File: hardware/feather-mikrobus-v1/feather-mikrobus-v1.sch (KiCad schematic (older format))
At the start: 24 parts, among them J1 Adafruit_Feather_socket_heade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, J2 Adafruit_Feather_socket_heade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, J3 mikroBUS_socket_header_left_p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, J4 mikroBUS_socket_header_right_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, SW1 C_and_K_JS102011SAQN, SW2 C_and_K_KMR421GULCLFS, SW3 C_and_K_KMR421GULCLFS

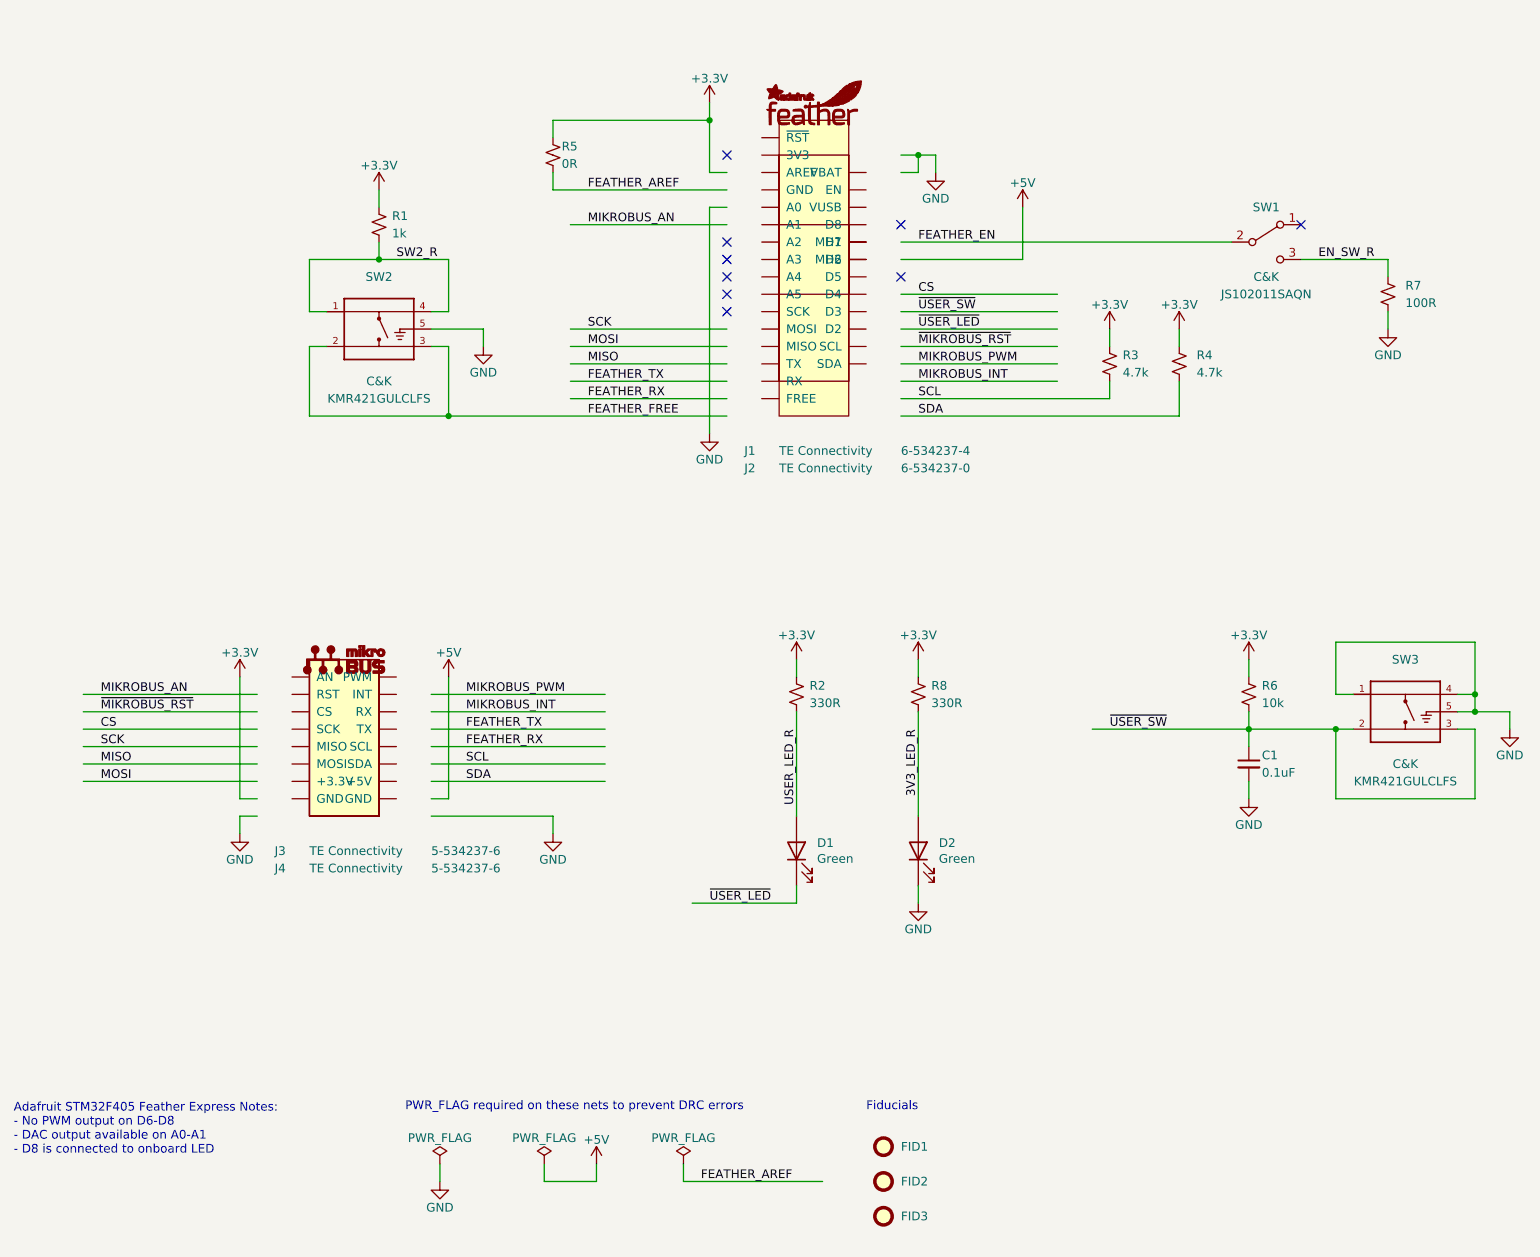
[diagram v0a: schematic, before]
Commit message: Update schematic to use new symbols and worksheet
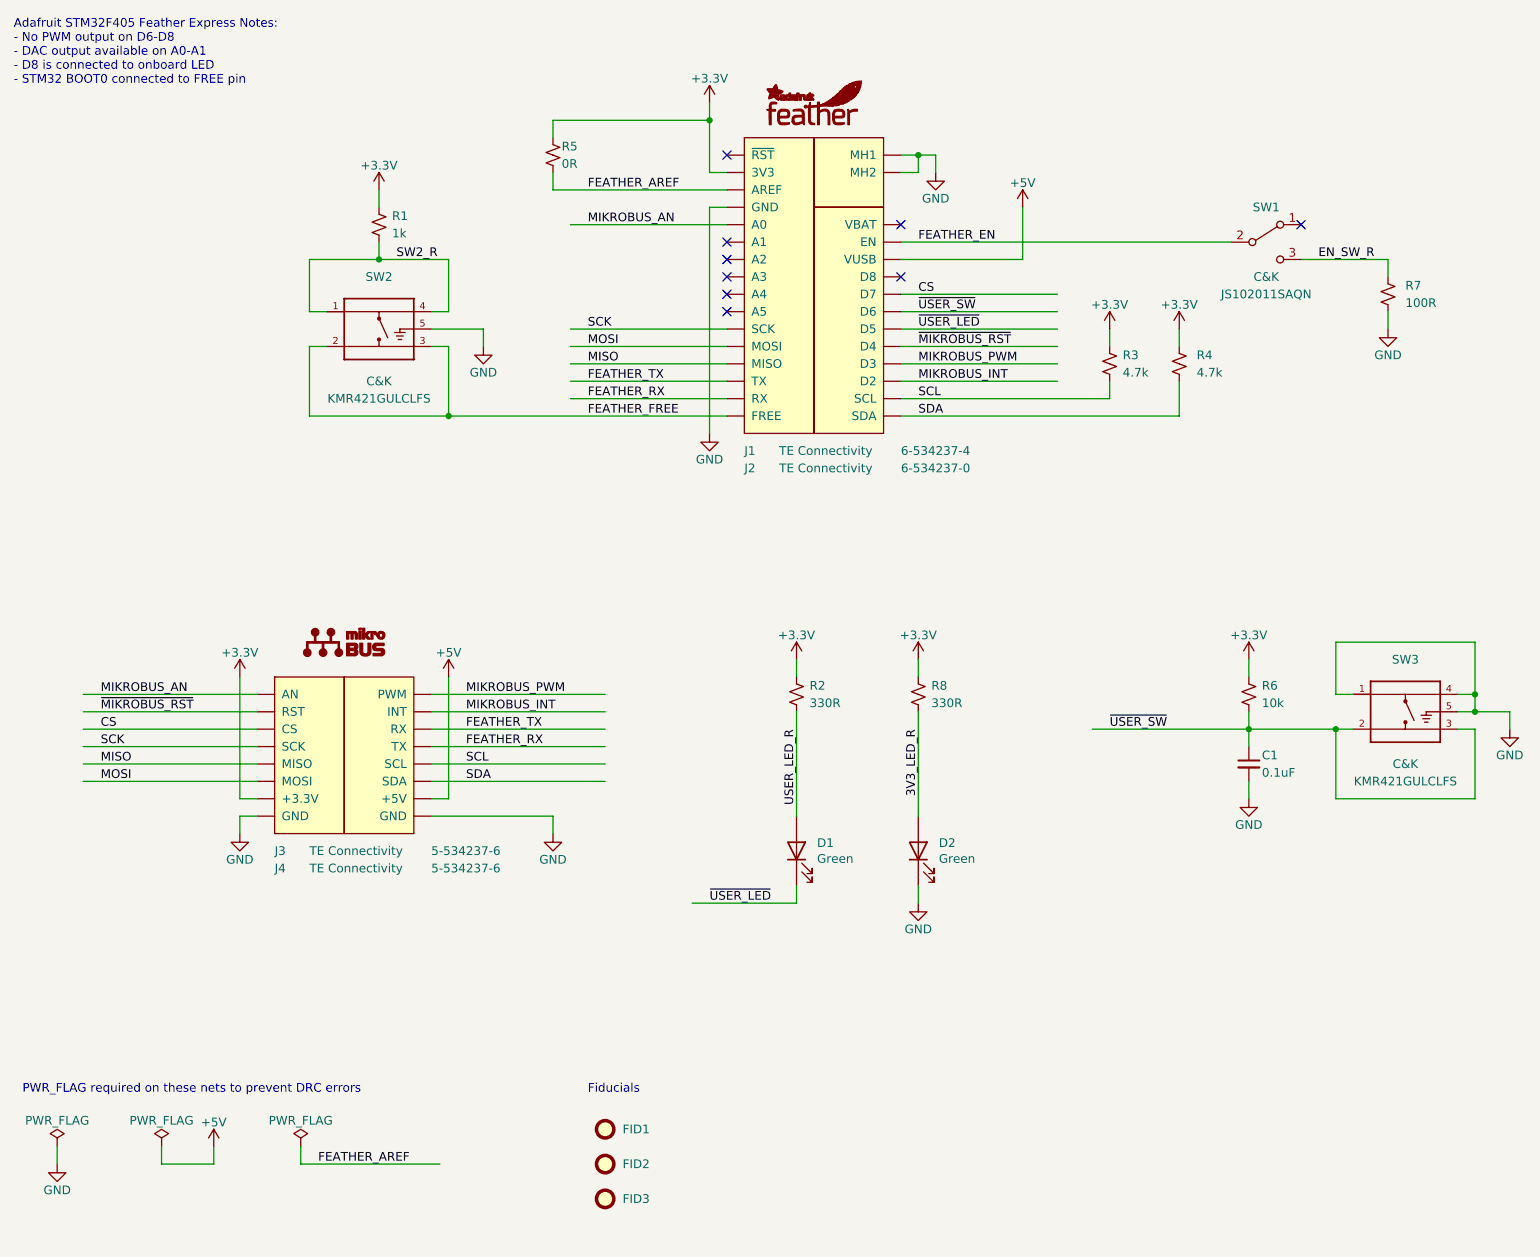
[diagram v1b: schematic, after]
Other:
- note added: "Adafruit STM32F405 Feather Express Notes:\n- No PWM output on D6-D8\n- DAC output available on A0-A1\n- D8 is connected to onboard LED\n- STM32 BOOT0 connected to FREE pin"
- note removed: "Adafruit STM32F405 Feather Express Notes:\n- No PWM output on D6-D8\n- DAC output available on A0-A1\n- D8 is connected to onboard LED"
- moved on the sheet: FID1, FID2, FID3, J1, J2, J3, J4

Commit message: Add Flying Camp Design logo
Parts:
- added LOGO?: Flying_Camp_Design_logo_30x30mm_silkscreen, Flying_Camp_Design:Flying_Camp_Design_logo_30x30mm_silkscreen, symbol Flying_Camp_Design:Flying_Camp_Design_logo_30x30mm_silkscreen
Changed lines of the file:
@@
 	0    -1   -1   0
 $EndComp
+$Comp
+L Flying_Camp_Design:Flying_Camp_Design_logo_30x30mm_silkscreen LOGO?
+U 1 1 5E6C1717
+P 5800 7400
+F 0 "LOGO?" H 5800 6830 60  0001 C CNN
+F 1 "Flying_Camp_Design_logo_30x30mm_silkscreen" H 5800 7970 60  0001 C CNN
+F 2 "Flying_Camp_Design:Flying_Camp_Design_logo_30x30mm_silkscreen" H 5800 7400 50  0001 C CNN
+F 3 "~" H 5800 7400 50  0001 C CNN
+	1    5800 7400
+	1    0    0    -1
+$EndComp
 $EndSCHEMATC

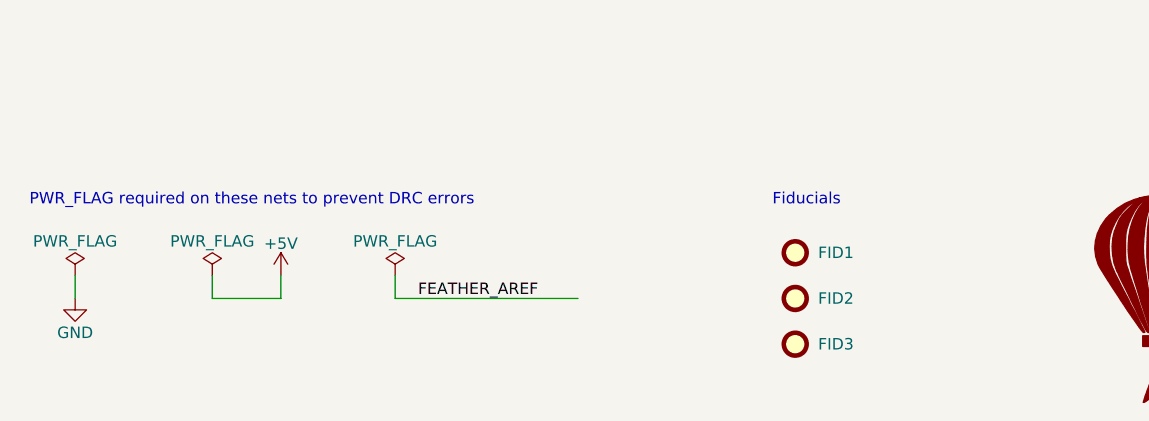
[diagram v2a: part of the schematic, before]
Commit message: Add Flying Camp Design logos
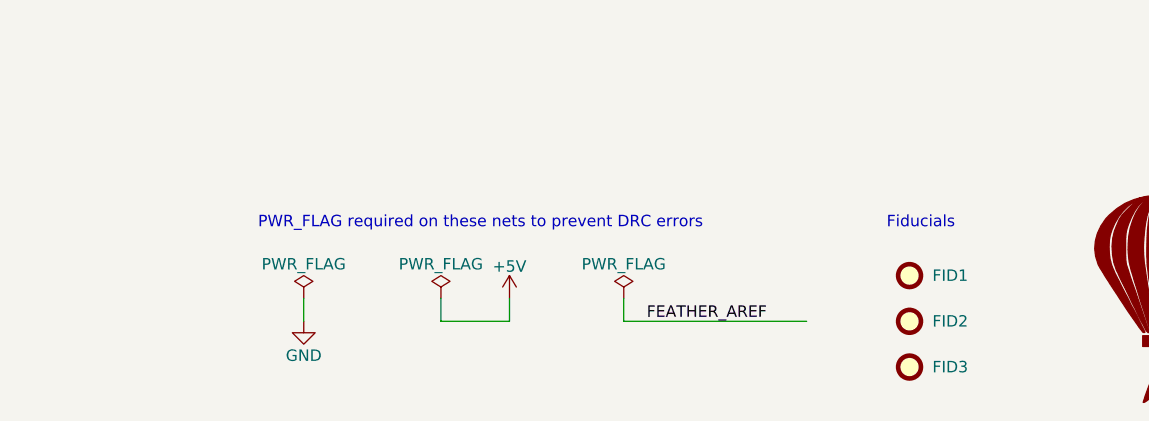
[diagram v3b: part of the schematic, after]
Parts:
- removed LOGO?: Flying_Camp_Design_logo_30x30mm_silkscreen, Flying_Camp_Design:Flying_Camp_Design_logo_30x30mm_silkscreen, symbol Flying_Camp_Design:Flying_Camp_Design_logo_30x30mm_silkscreen
- added LOGO2: Flying_Camp_Design_logo_7.35x11mm_silkscreen, Flying_Camp_Design:Flying_Camp_Design_logo_7.35x11mm_silkscreen, symbol Flying_Camp_Design:Flying_Camp_Design_logo_7.35x11mm_silkscreen
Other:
- moved on the sheet: FID1, FID2, FID3
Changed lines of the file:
@@
 $EndDescr
 Wire Wire Line
-	1950 7400 1950 7300
-Wire Wire Line
-	1650 7400 1950 7400
-Wire Wire Line
-	1650 7300 1650 7400
-Wire Wire Line
-	2450 7400 3250 7400
-Wire Wire Line
-	2450 7300 2450 7400
-Text Label 2550 7400 0    50   ~ 0
+	2950 7500 2950 7400
+Wire Wire Line
+	2650 7500 2950 7500
+Wire Wire Line
+	2650 7400 2650 7500
+Wire Wire Line
+	3450 7500 4250 7500
+Wire Wire Line
+	3450 7400 3450 7500
+Text Label 3550 7500 0    50   ~ 0
 FEATHER_AREF
 Wire Wire Line
@@
 Adafruit STM32F405 Feather Express Notes:\n- No PWM output on D6-D8\n- DAC output available on A0-A1\n- D8 is connected to onboard LED\n- STM32 BOOT0 connected to FREE pin
 Wire Wire Line
-	1050 7300 1050 7400
-Text Notes 850  7000 0    50   ~ 0
+	2050 7400 2050 7500
+Text Notes 1850 7100 0    50   ~ 0
 PWR_FLAG required on these nets to prevent DRC errors
 Wire Wire Line
@@
 Wire Wire Line
 	4900 1900 4800 1900
-Text Notes 4100 7000 0    50   ~ 0
+Text Notes 4600 7100 0    50   ~ 0
 Fiducials
 Wire Wire Line
@@
 L power:PWR_FLAG #FLG0103
 U 1 1 5E4EC363
-P 2450 7300
-F 0 "#FLG0103" H 2450 7375 50  0001 C CNN
-F 1 "PWR_FLAG" H 2450 7450 50  0000 C CNN
-F 2 "" H 2450 7300 50  0001 C CNN
-F 3 "~" H 2450 7300 50  0001 C CNN
-	1    2450 7300
+P 3450 7400
+F 0 "#FLG0103" H 3450 7475 50  0001 C CNN
+F 1 "PWR_FLAG" H 3450 7550 50  0000 C CNN
+F 2 "" H 3450 7400 50  0001 C CNN
+F 3 "~" H 3450 7400 50  0001 C CNN
+	1    3450 7400
 	1    0    0    -1
 $EndComp
@@
 L power:PWR_FLAG #FLG0102
 U 1 1 5E4548A0
-P 1650 7300
-F 0 "#FLG0102" H 1650 7375 50  0001 C CNN
-F 1 "PWR_FLAG" H 1650 7450 50  0000 C CNN
-F 2 "" H 1650 7300 50  0001 C CNN
-F 3 "~" H 1650 7300 50  0001 C CNN
-	1    1650 7300
+P 2650 7400
+F 0 "#FLG0102" H 2650 7475 50  0001 C CNN
+F 1 "PWR_FLAG" H 2650 7550 50  0000 C CNN
+F 2 "" H 2650 7400 50  0001 C CNN
+F 3 "~" H 2650 7400 50  0001 C CNN
+	1    2650 7400
 	1    0    0    -1
 $EndComp
@@
 L Flying_Camp_Design:+5V #PWR0102
 U 1 1 5E45585F
-P 1950 7300
-F 0 "#PWR0102" H 1950 7150 50  0001 C CNN
-F 1 "+5V" H 1950 7440 50  0000 C CNN
-F 2 "" H 1950 7300 50  0001 C CNN
-F 3 "" H 1950 7300 50  0001 C CNN
-	1    1950 7300
+P 2950 7400
+F 0 "#PWR0102" H 2950 7250 50  0001 C CNN
+F 1 "+5V" H 2950 7540 50  0000 C CNN
+F 2 "" H 2950 7400 50  0001 C CNN
+F 3 "" H 2950 7400 50  0001 C CNN
+	1    2950 7400
 	1    0    0    -1
 $EndComp
@@
 L power:GND #PWR0101
 U 1 1 5E455284
-P 1050 7400
-F 0 "#PWR0101" H 1050 7150 50  0001 C CNN
-F 1 "GND" H 1050 7250 50  0000 C CNN
-F 2 "" H 1050 7400 50  0001 C CNN
-F 3 "" H 1050 7400 50  0001 C CNN
-	1    1050 7400
+P 2050 7500
+F 0 "#PWR0101" H 2050 7250 50  0001 C CNN
+F 1 "GND" H 2050 7350 50  0000 C CNN
+F 2 "" H 2050 7500 50  0001 C CNN
+F 3 "" H 2050 7500 50  0001 C CNN
+	1    2050 7500
 	1    0    0    -1
 $EndComp
@@
 L power:PWR_FLAG #FLG0101
 U 1 1 5E454119
-P 1050 7300
-F 0 "#FLG0101" H 1050 7375 50  0001 C CNN
-F 1 "PWR_FLAG" H 1050 7450 50  0000 C CNN
-F 2 "" H 1050 7300 50  0001 C CNN
-F 3 "~" H 1050 7300 50  0001 C CNN
-	1    1050 7300
+P 2050 7400
+F 0 "#FLG0101" H 2050 7475 50  0001 C CNN
+F 1 "PWR_FLAG" H 2050 7550 50  0000 C CNN
+F 2 "" H 2050 7400 50  0001 C CNN
+F 3 "~" H 2050 7400 50  0001 C CNN
+	1    2050 7400
 	1    0    0    -1
 $EndComp
@@
 L Flying_Camp_Design:Fiducial_1mm_Mask2mm FID3
 U 1 1 5E3F3D03
-P 4200 7600
-F 0 "FID3" H 4300 7600 50  0000 L CNN
-F 1 "Fiducial_1mm_Mask2mm" H 4200 7500 50  0001 C CNN
-F 2 "Flying_Camp_Design:Fiducial_1mm_Mask2mm" H 4200 7400 50  0001 C CNN
-F 3 "~" H 4200 7300 50  0001 C CNN
-	1    4200 7600
+P 4700 7700
+F 0 "FID3" H 4800 7700 50  0000 L CNN
+F 1 "Fiducial_1mm_Mask2mm" H 4700 7600 50  0001 C CNN
+F 2 "Flying_Camp_Design:Fiducial_1mm_Mask2mm" H 4700 7500 50  0001 C CNN
+F 3 "~" H 4700 7400 50  0001 C CNN
+	1    4700 7700
 	1    0    0    -1
 $EndComp
@@
 L Flying_Camp_Design:Fiducial_1mm_Mask2mm FID2
 U 1 1 5E3F3A33
-P 4200 7400
-F 0 "FID2" H 4300 7400 50  0000 L CNN
-F 1 "Fiducial_1mm_Mask2mm" H 4200 7300 50  0001 C CNN
-F 2 "Flying_Camp_Design:Fiducial_1mm_Mask2mm" H 4200 7200 50  0001 C CNN
-F 3 "~" H 4200 7100 50  0001 C CNN
-	1    4200 7400
+P 4700 7500
+F 0 "FID2" H 4800 7500 50  0000 L CNN
+F 1 "Fiducial_1mm_Mask2mm" H 4700 7400 50  0001 C CNN
+F 2 "Flying_Camp_Design:Fiducial_1mm_Mask2mm" H 4700 7300 50  0001 C CNN
+F 3 "~" H 4700 7200 50  0001 C CNN
+	1    4700 7500
 	1    0    0    -1
 $EndComp
@@
 L Flying_Camp_Design:Fiducial_1mm_Mask2mm FID1
 U 1 1 5E3F32FE
-P 4200 7200
-F 0 "FID1" H 4300 7200 50  0000 L CNN
-F 1 "Fiducial_1mm_Mask2mm" H 4200 7100 50  0001 C CNN
-F 2 "Flying_Camp_Design:Fiducial_1mm_Mask2mm" H 4200 7000 50  0001 C CNN
-F 3 "~" H 4200 6900 50  0001 C CNN
-	1    4200 7200
+P 4700 7300
+F 0 "FID1" H 4800 7300 50  0000 L CNN
+F 1 "Fiducial_1mm_Mask2mm" H 4700 7200 50  0001 C CNN
+F 2 "Flying_Camp_Design:Fiducial_1mm_Mask2mm" H 4700 7100 50  0001 C CNN
+F 3 "~" H 4700 7000 50  0001 C CNN
+	1    4700 7300
 	1    0    0    -1
 $EndComp
@@
 $EndComp
 $Comp
-L Flying_Camp_Design:Flying_Camp_Design_logo_30x30mm_silkscreen LOGO?
-U 1 1 5E6C1717
+L Flying_Camp_Design:Flying_Camp_Design_logo_7.35x11mm_silkscreen LOGO2
+U 1 1 5E6E903B
 P 5800 7400
-F 0 "LOGO?" H 5800 6830 60  0001 C CNN
-F 1 "Flying_Camp_Design_logo_30x30mm_silkscreen" H 5800 7970 60  0001 C CNN
-F 2 "Flying_Camp_Design:Flying_Camp_Design_logo_30x30mm_silkscreen" H 5800 7400 50  0001 C CNN
+F 0 "LOGO2" H 5800 6830 60  0001 C CNN
+F 1 "Flying_Camp_Design_logo_7.35x11mm_silkscreen" H 5800 7970 60  0001 C CNN
+F 2 "Flying_Camp_Design:Flying_Camp_Design_logo_7.35x11mm_silkscreen" H 5800 7400 50  0001 C CNN
 F 3 "~" H 5800 7400 50  0001 C CNN
 	1    5800 7400
